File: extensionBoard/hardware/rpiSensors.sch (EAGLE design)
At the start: 31 parts, among them IC1 MEGA8-P

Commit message: minor
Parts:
- added C2, C4: (no value), capacitor-wima:C5/2.5
- added Q1: (no value), crystal:CRYSTALHC49S
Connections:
- removed net +5V: C3.2, IC1.AVCC, IC1.VCC@1, SV1.2, X1-2.KL, X2-2.KL, X3-2.KL, X4-2.KL, X5-2.KL, X6-2.KL
- new net +3V3: C3.2, IC1.VCC@1, SV1.1, X1-2.KL, X2-2.KL, X3-2.KL, X4-2.KL, X5-2.KL, X6-2.KL
- new net N$37: C2.2, IC1.PB6(XTAL1/TOSC1), Q1.2
- new net N$38: C4.2, IC1.PB7(XTAL2/TOSC2), Q1.1
- net GND: now also C2.1, C4.1

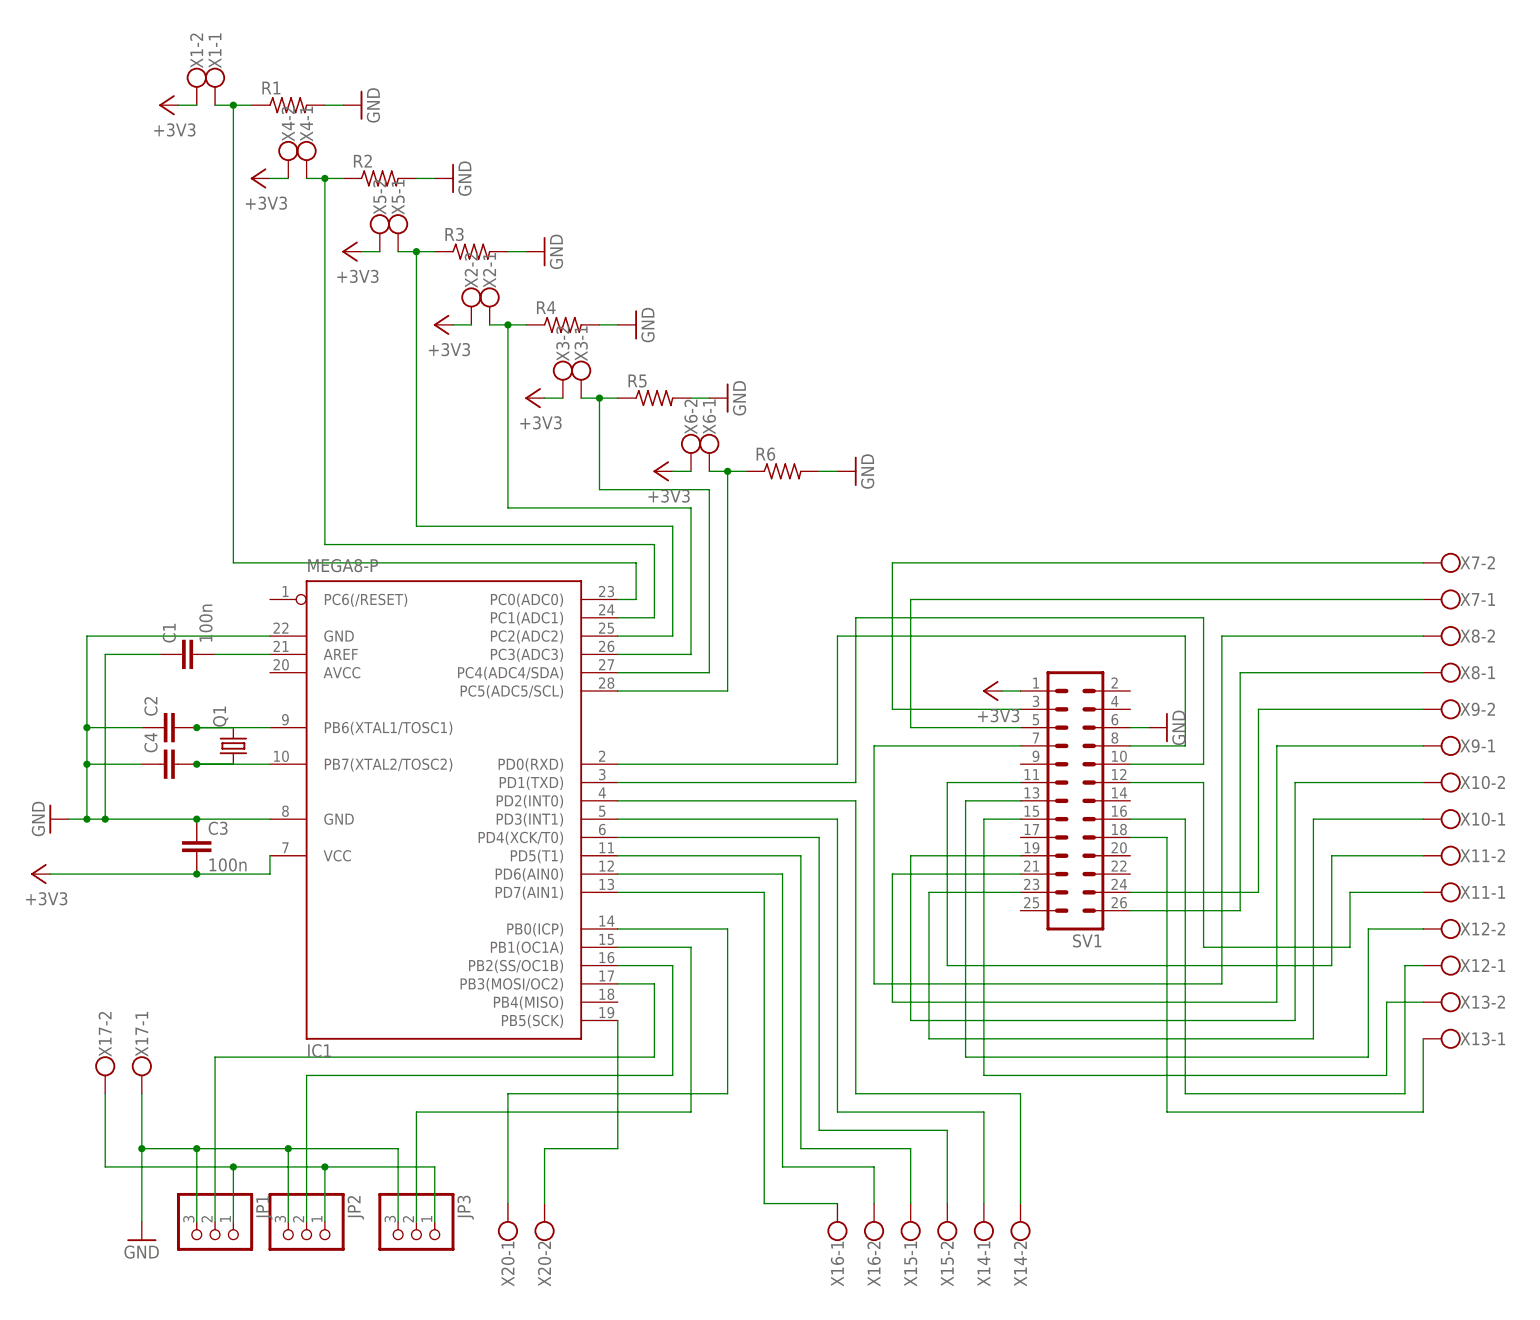
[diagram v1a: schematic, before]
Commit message: revived schematics
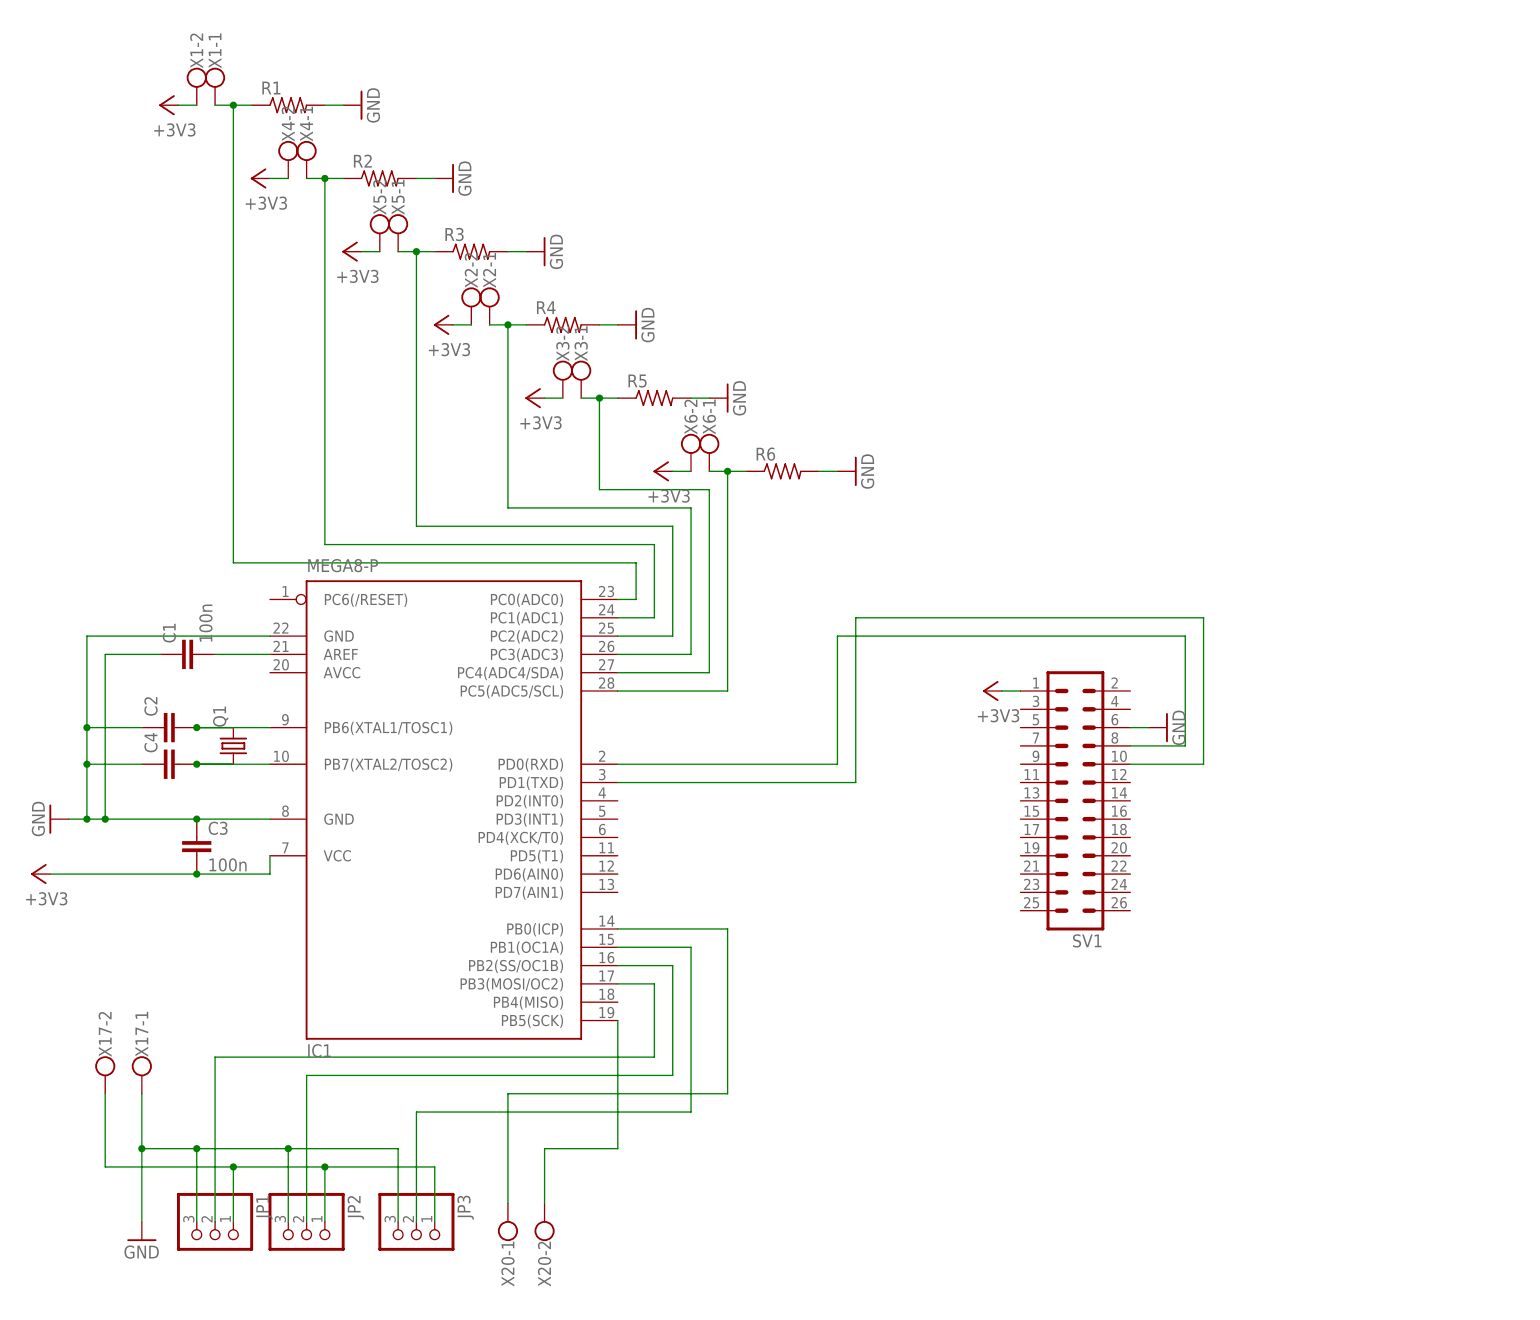
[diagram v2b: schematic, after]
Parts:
- removed X10, X11, X12, X13, X14, X15, X16, X7, X8, X9: (no value), con-wago-500:W237-102
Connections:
- removed net N$10: SV1.5, X7-1.KL
- removed net N$11: SV1.7, X8-2.KL
- removed net N$12: SV1.26, X8-1.KL
- removed net N$13: SV1.24, X9-2.KL
- removed net N$14: SV1.21, X9-1.KL
- removed net N$15: SV1.19, X10-2.KL
- removed net N$16: SV1.23, X10-1.KL
- removed net N$17: SV1.11, X11-2.KL
- removed net N$18: SV1.12, X11-1.KL
- removed net N$19: SV1.13, X12-2.KL
- removed net N$20: SV1.15, X13-2.KL
- removed net N$21: SV1.16, X12-1.KL
- removed net N$22: SV1.18, X13-1.KL
- removed net N$29: IC1.PD2(INT0), X14-2.KL
- removed net N$30: IC1.PD3(INT1), X14-1.KL
- removed net N$31: IC1.PD4(XCK/T0), X15-2.KL
- removed net N$32: IC1.PD5(T1), X15-1.KL
- removed net N$33: IC1.PD6(AIN0), X16-2.KL
- removed net N$34: IC1.PD7(AIN1), X16-1.KL
- removed net N$9: SV1.3, X7-2.KL
